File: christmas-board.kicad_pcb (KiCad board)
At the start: 2 copper layers, 96.2 x 96.2 mm, 47 parts, among them J1 Conn_01x02_Female, Q1 Q_NPN_EBC, Q2 Q_NPN_EBC, Q3 Q_NPN_EBC, Q4 Q_NPN_EBC, Q5 Q_NPN_EBC, SW1 SW_Push, SW2 SW_Push, U1 595_SHIFT, U2 555

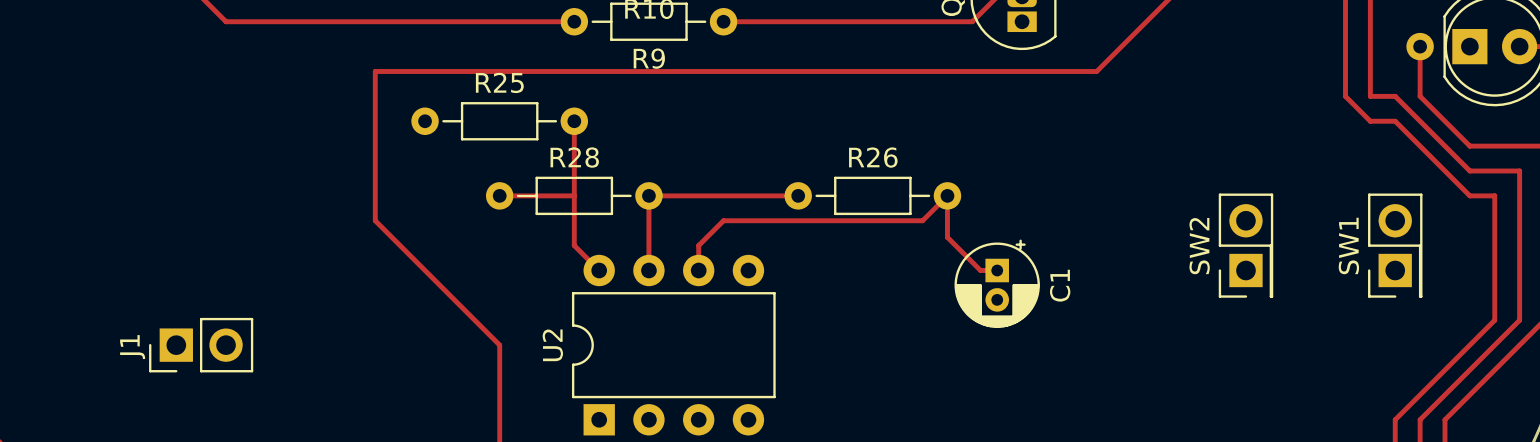
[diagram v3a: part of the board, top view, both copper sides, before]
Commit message: sw footprint added
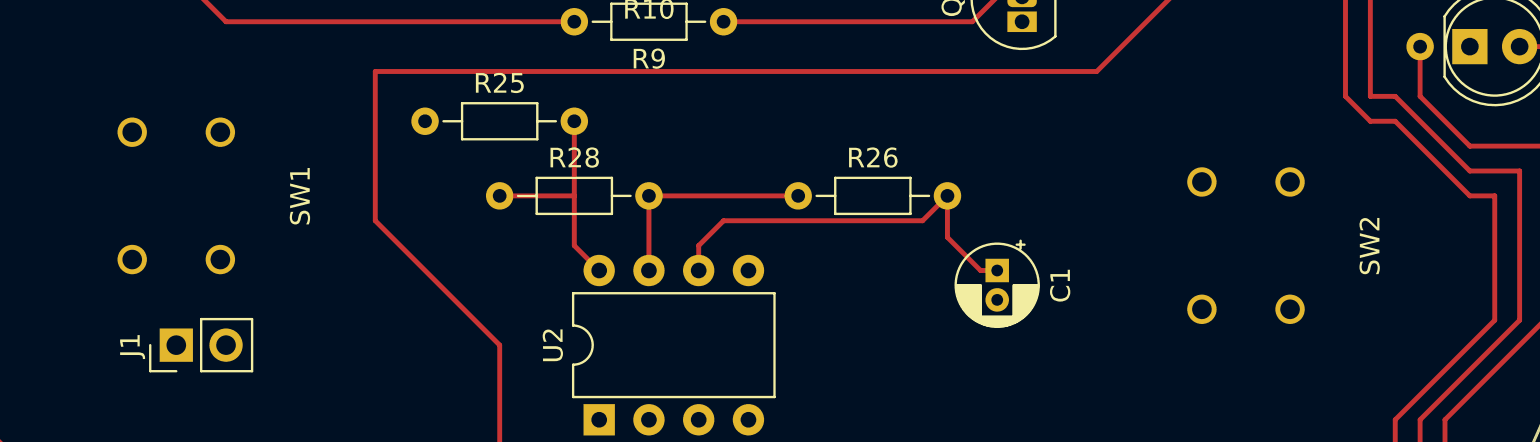
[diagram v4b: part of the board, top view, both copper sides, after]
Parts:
- SW1, SW2: footprint Connector_PinHeader_2.54mm:PinHeader_2x01_P2.54mm_Vertical -> christmas_board_footprint_lib:Tactile_Shallow_SW
- moved SW1 62.3 mm to (85.1, 96.5)
- moved SW2 1.27 mm to (139.7, 99.1)
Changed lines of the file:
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@@
     (pad_to_mask_clearance 0.2)
     (aux_axis_origin 0 0)
-    (visible_elements FFFFFF7F)
+    (visible_elements FFFFF77F)
     (pcbplotparams
       (layerselection 0x010fc_ffffffff)
@@
     (add_net "Net-(U2-Pad5)")
     (add_net VCC)
+  )
+  (module christmas_board_footprint_lib:Tactile_Shallow_SW (layer F.Cu)
+    (at 139.7 99.06 90)
+    (fp_text reference SW2 (at 0 6.35 90) (layer F.SilkS)
+      (effects (font (size 1 1) (thickness 0.15)))
+    )
+    (fp_text value SW_Push (at 0 -7.62 90) (layer F.Fab)
+      (effects (font (size 1 1) (thickness 0.15)))
+    )
+    (pad 2 thru_hole circle (at -3.25 2.25 90) (size 1.5 1.5) (drill 1) (layers *.Cu *.Mask)
+      (net 16 /PULL_HIGH))
+    (pad 2 thru_hole circle (at 3.25 2.25 90) (size 1.5 1.5) (drill 1) (layers *.Cu *.Mask)
+      (net 16 /PULL_HIGH))
+    (pad 1 thru_hole circle (at 3.25 -2.25 90) (size 1.5 1.5) (drill 1) (layers *.Cu *.Mask)
+      (net 2 GND))
+    (pad 1 thru_hole circle (at -3.25 -2.25 90) (size 1.5 1.5) (drill 1) (layers *.Cu *.Mask)
+      (net 2 GND))
+  )
+  (module christmas_board_footprint_lib:Tactile_Shallow_SW (layer F.Cu)
+    (at 85.09 96.52 90)
+    (fp_text reference SW1 (at 0 6.35 90) (layer F.SilkS)
+      (effects (font (size 1 1) (thickness 0.15)))
+    )
+    (fp_text value SW_Push (at 0 -7.62 90) (layer F.Fab)
+      (effects (font (size 1 1) (thickness 0.15)))
+    )
+    (pad 2 thru_hole circle (at -3.25 2.25 90) (size 1.5 1.5) (drill 1) (layers *.Cu *.Mask)
+      (net 16 /PULL_HIGH))
+    (pad 2 thru_hole circle (at 3.25 2.25 90) (size 1.5 1.5) (drill 1) (layers *.Cu *.Mask)
+      (net 16 /PULL_HIGH))
+    (pad 1 thru_hole circle (at 3.25 -2.25 90) (size 1.5 1.5) (drill 1) (layers *.Cu *.Mask)
+      (net 11 VCC))
+    (pad 1 thru_hole circle (at -3.25 -2.25 90) (size 1.5 1.5) (drill 1) (layers *.Cu *.Mask)
+      (net 11 VCC))
   )
   (module Capacitor_THT:CP_Radial_D4.0mm_P1.50mm (layer F.Cu)
@@
       (at (xyz 0 0 0))
       (scale (xyz 1 1 1))
-      (rotate (xyz 0 0 0))
-    )
-  )
-  (module Connector_PinHeader_2.54mm:PinHeader_2x01_P2.54mm_Vertical (layer F.Cu)
-    (at 147.32 100.33 90)
-    (descr "Through hole straight pin header, 2x01, 2.54mm pitch, double rows")
-    (tags "Through hole pin header THT 2x01 2.54mm double row")
-    (fp_text reference SW1 (at 1.27 -2.33 90) (layer F.SilkS)
-      (effects (font (size 1 1) (thickness 0.15)))
-    )
-    (fp_text value SW_Push (at 1.27 2.33 90) (layer F.Fab)
-      (effects (font (size 1 1) (thickness 0.15)))
-    )
-    (fp_line (start 0 -1.27) (end 3.81 -1.27) (layer F.Fab) (width 0.1))
-    (fp_line (start 3.81 -1.27) (end 3.81 1.27) (layer F.Fab) (width 0.1))
-    (fp_line (start 3.81 1.27) (end -1.27 1.27) (layer F.Fab) (width 0.1))
-    (fp_line (start -1.27 1.27) (end -1.27 0) (layer F.Fab) (width 0.1))
-    (fp_line (start -1.27 0) (end 0 -1.27) (layer F.Fab) (width 0.1))
-    (fp_line (start -1.33 1.33) (end 3.87 1.33) (layer F.SilkS) (width 0.12))
-    (fp_line (start -1.33 1.27) (end -1.33 1.33) (layer F.SilkS) (width 0.12))
-    (fp_line (start 3.87 -1.33) (end 3.87 1.33) (layer F.SilkS) (width 0.12))
-    (fp_line (start -1.33 1.27) (end 1.27 1.27) (layer F.SilkS) (width 0.12))
-    (fp_line (start 1.27 1.27) (end 1.27 -1.33) (layer F.SilkS) (width 0.12))
-    (fp_line (start 1.27 -1.33) (end 3.87 -1.33) (layer F.SilkS) (width 0.12))
-    (fp_line (start -1.33 0) (end -1.33 -1.33) (layer F.SilkS) (width 0.12))
-    (fp_line (start -1.33 -1.33) (end 0 -1.33) (layer F.SilkS) (width 0.12))
-    (fp_line (start -1.8 -1.8) (end -1.8 1.8) (layer F.CrtYd) (width 0.05))
-    (fp_line (start -1.8 1.8) (end 4.35 1.8) (layer F.CrtYd) (width 0.05))
-    (fp_line (start 4.35 1.8) (end 4.35 -1.8) (layer F.CrtYd) (width 0.05))
-    (fp_line (start 4.35 -1.8) (end -1.8 -1.8) (layer F.CrtYd) (width 0.05))
-    (fp_text user %R (at 1.27 0 180) (layer F.Fab)
-      (effects (font (size 1 1) (thickness 0.15)))
-    )
-    (pad 1 thru_hole rect (at 0 0 90) (size 1.7 1.7) (drill 1) (layers *.Cu *.Mask)
-      (net 11 VCC))
-    (pad 2 thru_hole oval (at 2.54 0 90) (size 1.7 1.7) (drill 1) (layers *.Cu *.Mask)
-      (net 16 /PULL_HIGH))
-    (model ${KISYS3DMOD}/Connector_PinHeader_2.54mm.3dshapes/PinHeader_2x01_P2.54mm_Vertical.wrl
-      (at (xyz 0 0 0))
-      (scale (xyz 1 1 1))
-      (rotate (xyz 0 0 0))
-    )
-  )
-  (module Connector_PinHeader_2.54mm:PinHeader_2x01_P2.54mm_Vertical (layer F.Cu)
-    (at 139.7 100.33 90)
-    (descr "Through hole straight pin header, 2x01, 2.54mm pitch, double rows")
-    (tags "Through hole pin header THT 2x01 2.54mm double row")
-    (fp_text reference SW2 (at 1.27 -2.33 90) (layer F.SilkS)
-      (effects (font (size 1 1) (thickness 0.15)))
-    )
-    (fp_text value SW_Push (at 1.27 2.33 90) (layer F.Fab)
-      (effects (font (size 1 1) (thickness 0.15)))
-    )
-    (fp_text user %R (at 1.27 0 180) (layer F.Fab)
-      (effects (font (size 1 1) (thickness 0.15)))
-    )
-    (fp_line (start 4.35 -1.8) (end -1.8 -1.8) (layer F.CrtYd) (width 0.05))
-    (fp_line (start 4.35 1.8) (end 4.35 -1.8) (layer F.CrtYd) (width 0.05))
-    (fp_line (start -1.8 1.8) (end 4.35 1.8) (layer F.CrtYd) (width 0.05))
-    (fp_line (start -1.8 -1.8) (end -1.8 1.8) (layer F.CrtYd) (width 0.05))
-    (fp_line (start -1.33 -1.33) (end 0 -1.33) (layer F.SilkS) (width 0.12))
-    (fp_line (start -1.33 0) (end -1.33 -1.33) (layer F.SilkS) (width 0.12))
-    (fp_line (start 1.27 -1.33) (end 3.87 -1.33) (layer F.SilkS) (width 0.12))
-    (fp_line (start 1.27 1.27) (end 1.27 -1.33) (layer F.SilkS) (width 0.12))
-    (fp_line (start -1.33 1.27) (end 1.27 1.27) (layer F.SilkS) (width 0.12))
-    (fp_line (start 3.87 -1.33) (end 3.87 1.33) (layer F.SilkS) (width 0.12))
-    (fp_line (start -1.33 1.27) (end -1.33 1.33) (layer F.SilkS) (width 0.12))
-    (fp_line (start -1.33 1.33) (end 3.87 1.33) (layer F.SilkS) (width 0.12))
-    (fp_line (start -1.27 0) (end 0 -1.27) (layer F.Fab) (width 0.1))
-    (fp_line (start -1.27 1.27) (end -1.27 0) (layer F.Fab) (width 0.1))
-    (fp_line (start 3.81 1.27) (end -1.27 1.27) (layer F.Fab) (width 0.1))
-    (fp_line (start 3.81 -1.27) (end 3.81 1.27) (layer F.Fab) (width 0.1))
-    (fp_line (start 0 -1.27) (end 3.81 -1.27) (layer F.Fab) (width 0.1))
-    (pad 2 thru_hole oval (at 2.54 0 90) (size 1.7 1.7) (drill 1) (layers *.Cu *.Mask)
-      (net 16 /PULL_HIGH))
-    (pad 1 thru_hole rect (at 0 0 90) (size 1.7 1.7) (drill 1) (layers *.Cu *.Mask)
-      (net 2 GND))
-    (model ${KISYS3DMOD}/Connector_PinHeader_2.54mm.3dshapes/PinHeader_2x01_P2.54mm_Vertical.wrl
-      (at (xyz 0 0 0))
-      (scale (xyz 1 1 1))

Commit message: initial routing complete
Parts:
- moved J1 43.8 mm to (128.3, 111.8)
- moved SW1 6.48 mm to (86.4, 102.9), turned to 180 degrees
- turned SW2 to 180 degrees
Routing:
- net GND: track 0.00 -> 380.2 mm
- net VCC: track 16.8 -> 183.3 mm
- net /PULL_HIGH: track 97.9 -> 145.6 mm
- net /LED_E: track 72.1 -> 112.4 mm
- net /XOR_IN_A: track 47.4 -> 84.5 mm, vias 0 -> 1
- net /555_OUT: track 0.00 -> 9.94 mm
- net Net-(C1-Pad1): track 20.4 -> 29.1 mm

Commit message: switch added, tracks updated
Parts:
- added SW3: SW_SPDT, Connector_PinHeader_2.54mm:PinHeader_1x03_P2.54mm_Vertical, B.Cu at (124.5, 106.7)
- J1: moved to B.Cu
- turned J1 to 270 degrees
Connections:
- J1 pad 1: VCC -> Net-(J1-Pad1)
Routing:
- net GND: track 380.2 -> 373.6 mm
- net Net-(J1-Pad1): track 0.00 -> 5.61 mm
- net VCC: track 183.3 -> 186.4 mm
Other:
- net class thick added: clearance 0.5, trace_width 0.5, via_dia 0.8, via_drill 0.4

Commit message: add battery holder
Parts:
- J1: footprint Connector_PinHeader_2.54mm:PinHeader_1x02_P2.54mm_Vertical -> christmas_board_footprint_lib:battery_holder_2468
- moved J1 10.2 mm to (133.3, 102.9), turned to 0 degrees
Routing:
- net GND: track 373.6 -> 382.8 mm
- net Net-(J1-Pad1): track 5.61 -> 11.7 mm
- net /LED_H: track 158.5 -> 157.1 mm
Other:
- outline, holes or cut-outs redrawn

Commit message: gerbers generated
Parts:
- SW3: moved to F.Cu
- turned SW3 to 90 degrees
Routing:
- added copper zone on B.Cu, net GND
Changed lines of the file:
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@@
     (visible_elements FFFFFF7F)
     (pcbplotparams
-      (layerselection 0x010fc_ffffffff)
-      (usegerberextensions false)
+      (layerselection 0x01030_ffffffff)
+      (usegerberextensions true)
       (usegerberattributes false)
       (usegerberadvancedattributes false)
@@
       (outputformat 1)
       (mirror false)
-      (drillshape 1)
+      (drillshape 0)
       (scaleselection 1)
-      (outputdirectory ""))
+      (outputdirectory "gerber/"))
   )
   (net 0 "")
@@
     )
   )
-  (module Connector_PinHeader_2.54mm:PinHeader_1x03_P2.54mm_Vertical (layer B.Cu)
-    (at 124.46 106.68 270)
+  (module Connector_PinHeader_2.54mm:PinHeader_1x03_P2.54mm_Vertical (layer F.Cu)
+    (at 124.46 106.68 90)
     (descr "Through hole straight pin header, 1x03, 2.54mm pitch, single row")
     (tags "Through hole pin header THT 1x03 2.54mm single row")
-    (fp_text reference SW3 (at 0 2.33 270) (layer B.SilkS)
-      (effects (font (size 1 1) (thickness 0.15)) (justify mirror))
-    )
-    (fp_text value SW_SPDT (at 0 -7.41 270) (layer B.Fab)
-      (effects (font (size 1 1) (thickness 0.15)) (justify mirror))
-    )
-    (fp_line (start -0.635 1.27) (end 1.27 1.27) (layer B.Fab) (width 0.1))
-    (fp_line (start 1.27 1.27) (end 1.27 -6.35) (layer B.Fab) (width 0.1))
-    (fp_line (start 1.27 -6.35) (end -1.27 -6.35) (layer B.Fab) (width 0.1))
-    (fp_line (start -1.27 -6.35) (end -1.27 0.635) (layer B.Fab) (width 0.1))
-    (fp_line (start -1.27 0.635) (end -0.635 1.27) (layer B.Fab) (width 0.1))
-    (fp_line (start -1.33 -6.41) (end 1.33 -6.41) (layer B.SilkS) (width 0.12))
-    (fp_line (start -1.33 -1.27) (end -1.33 -6.41) (layer B.SilkS) (width 0.12))
-    (fp_line (start 1.33 -1.27) (end 1.33 -6.41) (layer B.SilkS) (width 0.12))
-    (fp_line (start -1.33 -1.27) (end 1.33 -1.27) (layer B.SilkS) (width 0.12))
-    (fp_line (start -1.33 0) (end -1.33 1.33) (layer B.SilkS) (width 0.12))
-    (fp_line (start -1.33 1.33) (end 0 1.33) (layer B.SilkS) (width 0.12))
-    (fp_line (start -1.8 1.8) (end -1.8 -6.85) (layer B.CrtYd) (width 0.05))
-    (fp_line (start -1.8 -6.85) (end 1.8 -6.85) (layer B.CrtYd) (width 0.05))
-    (fp_line (start 1.8 -6.85) (end 1.8 1.8) (layer B.CrtYd) (width 0.05))
-    (fp_line (start 1.8 1.8) (end -1.8 1.8) (layer B.CrtYd) (width 0.05))
-    (fp_text user %R (at 0 -2.54 180) (layer B.Fab)
-      (effects (font (size 1 1) (thickness 0.15)) (justify mirror))
-    )
-    (pad 1 thru_hole rect (at 0 0 270) (size 1.7 1.7) (drill 1) (layers *.Cu *.Mask)
+    (fp_text reference SW3 (at 0 -2.33 90) (layer F.SilkS)
+      (effects (font (size 1 1) (thickness 0.15)))
+    )
+    (fp_text value SW_SPDT (at 0 7.41 90) (layer F.Fab)
+      (effects (font (size 1 1) (thickness 0.15)))
+    )
+    (fp_line (start -0.635 -1.27) (end 1.27 -1.27) (layer F.Fab) (width 0.1))
+    (fp_line (start 1.27 -1.27) (end 1.27 6.35) (layer F.Fab) (width 0.1))
+    (fp_line (start 1.27 6.35) (end -1.27 6.35) (layer F.Fab) (width 0.1))
+    (fp_line (start -1.27 6.35) (end -1.27 -0.635) (layer F.Fab) (width 0.1))
+    (fp_line (start -1.27 -0.635) (end -0.635 -1.27) (layer F.Fab) (width 0.1))
+    (fp_line (start -1.33 6.41) (end 1.33 6.41) (layer F.SilkS) (width 0.12))
+    (fp_line (start -1.33 1.27) (end -1.33 6.41) (layer F.SilkS) (width 0.12))
+    (fp_line (start 1.33 1.27) (end 1.33 6.41) (layer F.SilkS) (width 0.12))
+    (fp_line (start -1.33 1.27) (end 1.33 1.27) (layer F.SilkS) (width 0.12))
+    (fp_line (start -1.33 0) (end -1.33 -1.33) (layer F.SilkS) (width 0.12))
+    (fp_line (start -1.33 -1.33) (end 0 -1.33) (layer F.SilkS) (width 0.12))
+    (fp_line (start -1.8 -1.8) (end -1.8 6.85) (layer F.CrtYd) (width 0.05))
+    (fp_line (start -1.8 6.85) (end 1.8 6.85) (layer F.CrtYd) (width 0.05))
+    (fp_line (start 1.8 6.85) (end 1.8 -1.8) (layer F.CrtYd) (width 0.05))
+    (fp_line (start 1.8 -1.8) (end -1.8 -1.8) (layer F.CrtYd) (width 0.05))
+    (fp_text user %R (at 0 2.54 180) (layer F.Fab)
+      (effects (font (size 1 1) (thickness 0.15)))
+    )
+    (pad 1 thru_hole rect (at 0 0 90) (size 1.7 1.7) (drill 1) (layers *.Cu *.Mask)
       (net 37 "Net-(SW3-Pad1)"))
-    (pad 2 thru_hole oval (at 0 -2.54 270) (size 1.7 1.7) (drill 1) (layers *.Cu *.Mask)
+    (pad 2 thru_hole oval (at 0 2.54 90) (size 1.7 1.7) (drill 1) (layers *.Cu *.Mask)
       (net 11 VCC))
-    (pad 3 thru_hole oval (at 0 -5.08 270) (size 1.7 1.7) (drill 1) (layers *.Cu *.Mask)
+    (pad 3 thru_hole oval (at 0 5.08 90) (size 1.7 1.7) (drill 1) (layers *.Cu *.Mask)
       (net 36 "Net-(J1-Pad1)"))
     (model ${KISYS3DMOD}/Connector_PinHeader_2.54mm.3dshapes/PinHeader_1x03_P2.54mm_Vertical.wrl
@@
   (segment (start 133.35 102.87) (end 129.54 106.68) (width 0.25) (layer F.Cu) (net 36))
   (segment (start 133.35 96.52) (end 133.35 102.87) (width 0.25) (layer F.Cu) (net 36))
+  (zone (net 2) (net_name GND) (layer B.Cu) (hatch edge 0.508)
+    (connect_pads (clearance 0.508))
+    (min_thickness 0.254)
+    (fill yes (arc_segments 16) (thermal_gap 0.508) (thermal_bridge_width 0.508))
+    (polygon
+      (pts
+        (xy 60 35) (xy 160 35) (xy 160 140) (xy 60 140) (xy 60 95)
+      )
+    )
+  )
 )
